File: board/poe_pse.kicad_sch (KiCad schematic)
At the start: 35 parts, among them Q1 SSM3K361R, Q2 SSM3K361R, Q3 SSM3K361R, Q4 SSM3K361R, U1 TPS23861

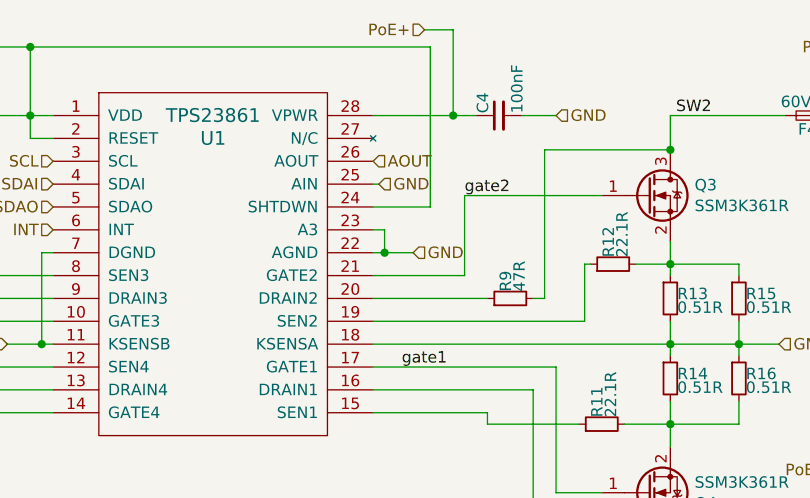
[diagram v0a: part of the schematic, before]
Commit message: broke out address lines
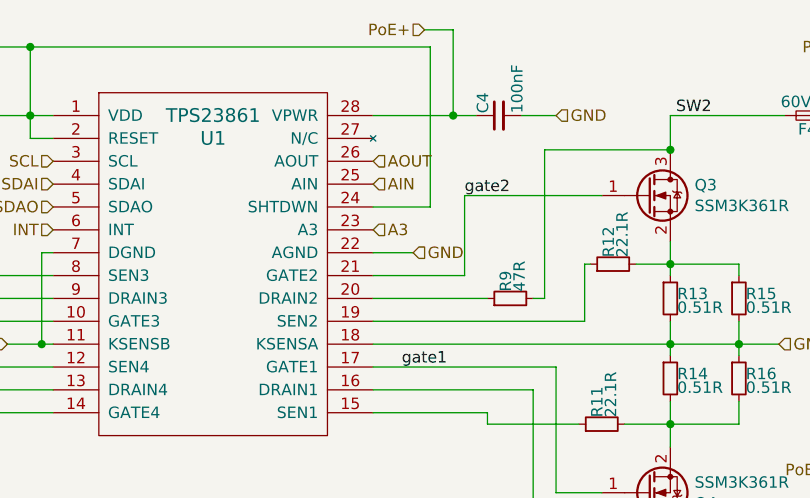
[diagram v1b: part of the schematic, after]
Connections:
- net GND: no longer U1.23 (A3), U1.25 (AIN)
- new net A3: U1.23 (A3)
- new net AIN: U1.25 (AIN)
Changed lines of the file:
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@@
   (junction (at 100.965 78.74) (diameter 0) (color 0 0 0 0)
   )
-  (junction (at 178.435 76.2) (diameter 0) (color 0 0 0 0)
-  )
   (junction (at 92.075 68.58) (diameter 0) (color 0 0 0 0)
   )
@@
     (stroke (width 0) (type default) (color 0 0 0 0))
   )
-  (wire (pts (xy 177.165 73.66) (xy 178.435 73.66))
-    (stroke (width 0) (type default) (color 0 0 0 0))
-  )
   (wire (pts (xy 108.585 78.74) (xy 112.395 78.74))
     (stroke (width 0) (type default) (color 0 0 0 0))
@@
     (stroke (width 0) (type default) (color 0 0 0 0))
   )
-  (wire (pts (xy 178.435 76.2) (xy 181.61 76.2))
+  (wire (pts (xy 177.165 76.2) (xy 181.61 76.2))
     (stroke (width 0) (type default) (color 0 0 0 0))
   )
@@
     (stroke (width 0) (type default) (color 0 0 0 0))
   )
-  (wire (pts (xy 177.165 68.58) (xy 177.8 68.58))
-    (stroke (width 0) (type default) (color 0 0 0 0))
-  )
   (wire (pts (xy 66.675 86.36) (xy 56.515 86.36))
     (stroke (width 0) (type default) (color 0 0 0 0))
@@
     (stroke (width 0) (type default) (color 0 0 0 0))
   )
-  (wire (pts (xy 177.165 76.2) (xy 178.435 76.2))
-    (stroke (width 0) (type default) (color 0 0 0 0))
-  )
-  (wire (pts (xy 178.435 73.66) (xy 178.435 76.2))
-    (stroke (width 0) (type default) (color 0 0 0 0))
-  )
   (wire (pts (xy 222.885 60.96) (xy 210.185 60.96))
     (stroke (width 0) (type default) (color 0 0 0 0))
@@
     (effects (font (size 1.27 1.27)) (justify left))
   )
+  (hierarchical_label "A3" (shape input) (at 177.165 73.66 0)
+    (effects (font (size 1.27 1.27)) (justify left))
+  )
   (hierarchical_label "SDAI" (shape input) (at 141.605 68.58 180)
     (effects (font (size 1.27 1.27)) (justify right))
@@
     (effects (font (size 1.27 1.27)) (justify right))
   )
-  (hierarchical_label "GND" (shape input) (at 177.8 68.58 0)
-    (effects (font (size 1.27 1.27)) (justify left))
-  )
+  (hierarchical_label "AIN" (shape input) (at 177.165 68.58 0)
+    (effects (font (size 1.27 1.27)) (justify left))
+  )

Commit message: moved symbol to local library
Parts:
- U1: symbol Auto-Intern:TPS23861 -> b115:TPS23861

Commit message: added lcsc part numbers
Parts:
- C1, C2, C4, C5, C6: lcsc (none) -> C14663
- C3: footprint Capacitor_SMD:C_0402_1005Metric -> Capacitor_SMD:C_0603_1608Metric; lcsc (none) -> C14663
- D1, D2, D3, D4: lcsc (none) -> C157526
- F1, F2, F3, F4: lcsc (none) -> C70066
- Q1, Q2, Q3, Q4: lcsc (none) -> C5444678
- R1, R13, R14, R15, R16, R2, R5, R6: lcsc (none) -> C705480
- R10, R3, R7, R9: lcsc (none) -> C23182
- R11, R12, R4, R8: lcsc (none) -> C22958
- U1: lcsc (none) -> C93245
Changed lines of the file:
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@@
+      (effects (font (size 1.27 1.27)) hide)
+    )
+    (property "lcsc" "C22958" (at 203.835 77.47 0)
       (effects (font (size 1.27 1.27)) hide)
     )
@@
       (effects (font (size 1.27 1.27)) hide)
     )
+    (property "lcsc" "C22958" (at 202.565 95.25 0)
+      (effects (font (size 1.27 1.27)) hide)
+    )
     (pin "1")
     (pin "2")
@@
     )
     (property "Datasheet" "~" (at 207.645 102.87 0)
+      (effects (font (size 1.27 1.27)) hide)
+    )
+    (property "lcsc" "C5444678" (at 207.645 102.87 0)
       (effects (font (size 1.27 1.27)) hide)
     )
@@
       (effects (font (size 1.27 1.27)) hide)
     )
+    (property "lcsc" "C70066" (at 225.425 60.96 0)
+      (effects (font (size 1.27 1.27)) hide)
+    )
     (pin "1")
     (pin "2")
@@
       (effects (font (size 1.27 1.27)) hide)
     )
+    (property "lcsc" "C23182" (at 111.125 68.58 0)
+      (effects (font (size 1.27 1.27)) hide)
+    )
     (pin "1")
     (pin "2")
@@
       (effects (font (size 1.27 1.27)) hide)
     )
+    (property "lcsc" "C23182" (at 192.405 81.28 0)
+      (effects (font (size 1.27 1.27)) hide)
+    )
     (pin "1")
     (pin "2")
@@
       (effects (font (size 1.27 1.27)) hide)
     )
+    (property "lcsc" "C22958" (at 114.935 78.74 0)
+      (effects (font (size 1.27 1.27)) hide)
+    )
     (pin "1")
     (pin "2")
@@
       (effects (font (size 1.27 1.27)) hide)
     )
+    (property "lcsc" "C705480" (at 100.965 82.55 0)
+      (effects (font (size 1.27 1.27)) hide)
+    )
     (pin "1")
     (pin "2")
@@
       (effects (font (size 1.27 1.27)) hide)
     )
+    (property "lcsc" "C14663" (at 240.665 104.14 0)
+      (effects (font (size 1.27 1.27)) hide)
+    )
     (pin "1")
     (pin "2")
@@
     )
     (property "Datasheet" "https://diotec.com/tl_files/diotec/files/pdf/datasheets/5kp65.pdf" (at 92.075 62.23 0)
+      (effects (font (size 1.27 1.27)) hide)
+    )
+    (property "lcsc" "C157526" (at 92.075 63.5 0)
       (effects (font (size 1.27 1.27)) hide)
     )
@@
     )
     (property "Digi-Key_PN" "296-37969-5-ND" (at 159.385 78.74 0)
+      (effects (font (size 1.27 1.27)) hide)
+    )
+    (property "lcsc" "C93245" (at 159.385 78.74 0)
       (effects (font (size 1.27 1.27)) hide)
     )
@@
       (effects (font (size 1.27 1.27)) hide)
     )
+    (property "lcsc" "C14663" (at 56.515 80.01 0)
+      (effects (font (size 1.27 1.27)) hide)
+    )
     (pin "1")
     (pin "2")
@@
       (effects (font (size 1.27 1.27)) hide)
     )
+    (property "lcsc" "C705480" (at 83.185 100.33 0)
+      (effects (font (size 1.27 1.27)) hide)
+    )
     (pin "1")
     (pin "2")
@@
       (effects (font (size 1.27 1.27)) hide)
     )
+    (property "lcsc" "C705480" (at 217.805 90.17 0)
+      (effects (font (size 1.27 1.27)) hide)
+    )
     (pin "1")
     (pin "2")
@@
     )
     (property "Tolerance" "1%" (at 210.185 90.17 0)
+      (effects (font (size 1.27 1.27)) hide)
+    )
+    (property "lcsc" "C705480" (at 210.185 90.17 0)
       (effects (font (size 1.27 1.27)) hide)
     )
@@
       (effects (font (size 1.27 1.27)) hide)
     )
+    (property "lcsc" "C70066" (at 222.885 107.95 0)
+      (effects (font (size 1.27 1.27)) hide)
+    )
     (pin "1")
     (pin "2")
@@
       (effects (font (size 1.27 1.27)) hide)
     )
+    (property "lcsc" "C157526" (at 66.675 80.01 0)
+      (effects (font (size 1.27 1.27)) hide)
+    )
     (pin "1")
     (pin "2")
@@
       (effects (font (size 1.27 1.27)) (justify left))
     )
-    (property "Footprint" "Capacitor_SMD:C_0402_1005Metric" (at 132.715 60.96 0)
+    (property "Footprint" "Capacitor_SMD:C_0603_1608Metric" (at 132.715 60.96 0)
       (effects (font (size 1.27 1.27)) hide)
     )
@@
       (effects (font (size 1.27 1.27)) hide)
     )
+    (property "lcsc" "C14663" (at 132.715 60.96 0)
+      (effects (font (size 1.27 1.27)) hide)
+    )
     (pin "1")
     (pin "2")
@@
       (effects (font (size 1.27 1.27)) hide)
     )
+    (property "lcsc" "C23182" (at 198.755 107.95 0)
+      (effects (font (size 1.27 1.27)) hide)
+    )
     (pin "1")
     (pin "2")
@@
     )
     (property "Tolerance" "1%" (at 210.185 81.28 0)
+      (effects (font (size 1.27 1.27)) hide)
+    )
+    (property "lcsc" "C705480" (at 210.185 81.28 0)
       (effects (font (size 1.27 1.27)) hide)
     )
@@
       (effects (font (size 1.27 1.27)) hide)
     )
+    (property "lcsc" "C70066" (at 70.485 86.36 0)
+      (effects (font (size 1.27 1.27)) hide)
+    )
     (pin "1")
     (pin "2")
@@
       (effects (font (size 1.27 1.27)) hide)
     )
+    (property "lcsc" "C22958" (at 89.535 96.52 0)
+      (effects (font (size 1.27 1.27)) hide)
+    )
     (pin "1")
     (pin "2")
@@
       (effects (font (size 1.27 1.27)) hide)
     )
+    (property "lcsc" "C157526" (at 233.045 57.15 0)
+      (effects (font (size 1.27 1.27)) hide)
+    )
     (pin "1")
     (pin "2")
@@
       (effects (font (size 1.27 1.27)) hide)
     )
+    (property "lcsc" "C705480" (at 75.565 100.33 0)
+      (effects (font (size 1.27 1.27)) hide)
+    )
     (pin "1")
     (pin "2")
@@
       (effects (font (size 1.27 1.27)) hide)
     )
+    (property "lcsc" "C14663" (at 80.645 63.5 0)
+      (effects (font (size 1.27 1.27)) hide)
+    )
     (pin "1")
     (pin "2")
@@
       (effects (font (size 1.27 1.27)) hide)
     )
+    (property "lcsc" "C705480" (at 217.805 81.28 0)
+      (effects (font (size 1.27 1.27)) hide)
+    )
     (pin "1")
     (pin "2")
@@
       (effects (font (size 1.27 1.27)) hide)
     )
+    (property "lcsc" "C5444678" (at 207.645 69.85 0)
+      (effects (font (size 1.27 1.27)) hide)
+    )
     (pin "1")
     (pin "2")
@@
       (effects (font (size 1.27 1.27)) hide)
     )
+    (property "lcsc" "C14663" (at 191.135 60.96 0)
+      (effects (font (size 1.27 1.27)) hide)
+    )
     (pin "1")
     (pin "2")
@@
     )
     (property "Datasheet" "~" (at 78.105 91.44 0)
+      (effects (font (size 1.27 1.27)) hide)
+    )
+    (property "lcsc" "C5444678" (at 78.105 91.44 0)
       (effects (font (size 1.27 1.27)) hide)
     )
@@
       (effects (font (size 1.27 1.27)) hide)
     )
+    (property "lcsc" "C70066" (at 95.885 68.58 0)
+      (effects (font (size 1.27 1.27)) hide)
+    )
     (pin "1")
     (pin "2")
@@
       (effects (font (size 1.27 1.27)) hide)
     )
+    (property "lcsc" "C14663" (at 243.205 57.15 0)
+      (effects (font (size 1.27 1.27)) hide)
+    )
     (pin "1")
     (pin "2")
@@
       (effects (font (size 1.27 1.27)) hide)
     )
+    (property "lcsc" "C705480" (at 108.585 82.55 0)
+      (effects (font (size 1.27 1.27)) hide)
+    )
     (pin "1")
     (pin "2")
@@
       (effects (font (size 1.27 1.27)) hide)
     )
+    (property "lcsc" "C5444678" (at 103.505 73.66 0)
+      (effects (font (size 1.27 1.27)) hide)
+    )
     (pin "1")
     (pin "2")
@@
       (effects (font (size 1.27 1.27)) hide)
     )
+    (property "lcsc" "C23182" (at 85.725 86.36 0)
+      (effects (font (size 1.27 1.27)) hide)
+    )
     (pin "1")
     (pin "2")
@@
       (effects (font (size 1.27 1.27)) hide)
     )
+    (property "lcsc" "C157526" (at 230.505 104.14 0)
+      (effects (font (size 1.27 1.27)) hide)
+    )
